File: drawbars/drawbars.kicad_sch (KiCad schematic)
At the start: 49 parts, among them J1 8-215079-6, J2 8-215079-6, J3 8-215079-6, Q1 BC547, U1 4051, U2 4051, U3 74HC04

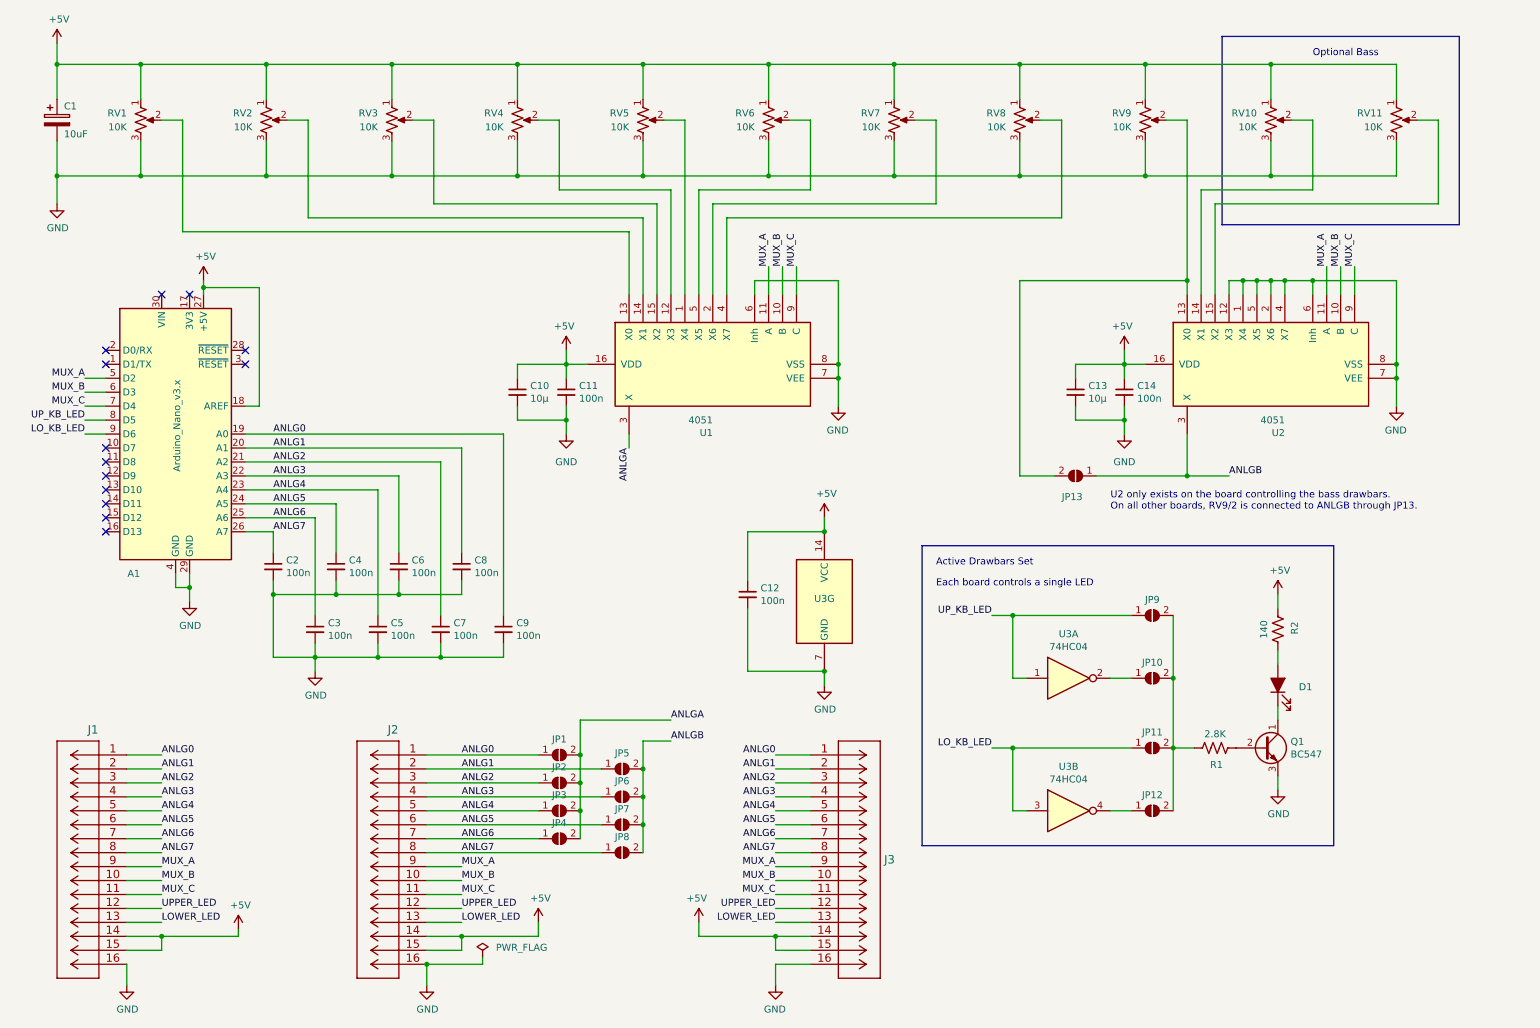
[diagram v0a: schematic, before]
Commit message: Drawbars Rev 1.1
On schematics : UP_REG_LED and LO_REG_LED signals were not routed to connectors.
Connectors pins assignments modified.
On PCB : Cutting line width increased. PCB width smaller for better drawbars 8 digit visibility when drawbars are pulled to max.
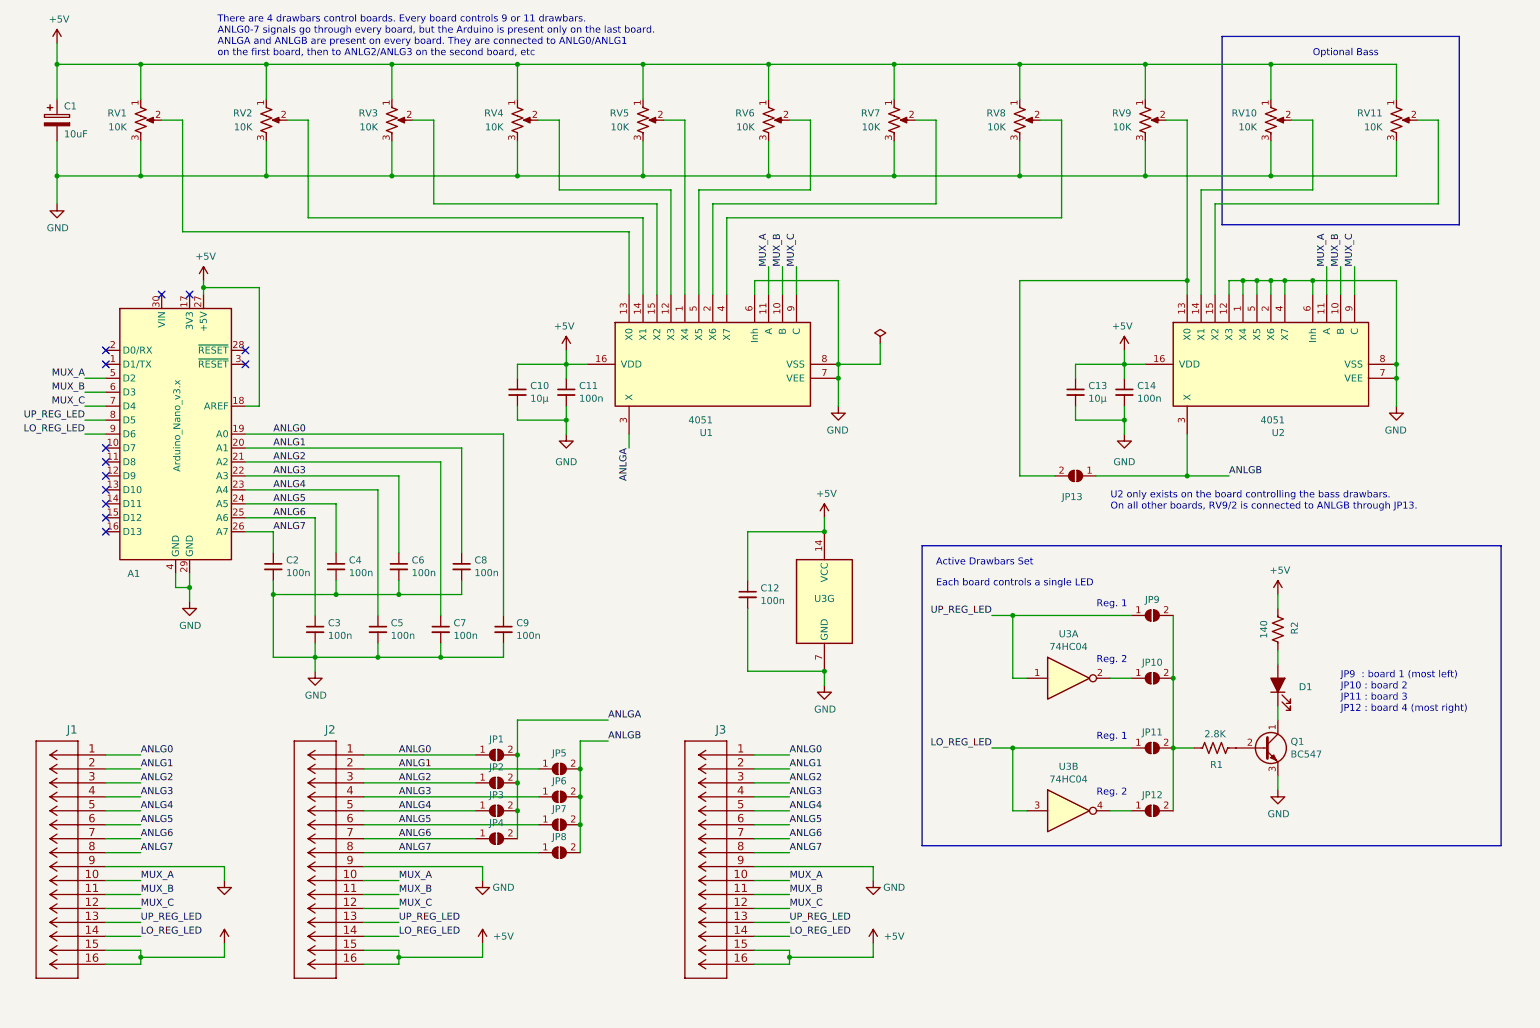
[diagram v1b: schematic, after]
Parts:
- J1, J3: value 8-215079-6 -> (none); footprint b3_footprints:MicroMatch_2x08_P1.27mm_Vertical -> (none)
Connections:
- net UPPER_LED is gone; now on net MUX_C: J1.12, J2.12, J3.12
- net UP_KB_LED is gone; now on net UP_REG_LED: A1.8 (D5), JP9.1 (A), U3.1
- net +5V: now also J1.16, J2.16, J3.16; no longer J1.14, J2.14, J3.14
- net GND: now also J1.9, J2.9, J3.9; no longer J1.16, J2.16, J3.16
- net MUX_A: now also J1.10, J2.10, J3.10; no longer J1.9, J2.9, J3.9
- net MUX_B: now also J1.11, J2.11, J3.11; no longer J1.10, J2.10, J3.10
- net MUX_C: no longer J1.11, J2.11, J3.11
- net LOWER_LED renamed UP_REG_LED
- net LO_KB_LED renamed LO_REG_LED
- net LO_REG_LED: now also J1.14, J2.14, J3.14
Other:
- note added: "JP9 : board 1 (most left) JP10 : board 2 JP11 : board 3 JP12 : board 4 (most right)"
- note added: "Reg. 1"
- note added: "Reg. 2"
- note added: "There are 4 drawbars control boards. Every board controls 9 or 11 drawbars. ANLG0-7 signals go through every board, but the Arduino is present only on the last board. ANLGA and ANLGB are present on every board. They are connected to ANLG0/ANLG1 on the first board, then to ANLG2/ANLG3 on the second board, etc"
- moved on the sheet: J1, J2, JP1, JP2, JP3, JP4, JP5, JP6, JP7, JP8

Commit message: Files updated to Kicad 8.0
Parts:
- J1, J3: value (none) -> 8-215079-6; footprint (none) -> b3_footprints:MicroMatch_2x08_P1.27mm_Vertical
